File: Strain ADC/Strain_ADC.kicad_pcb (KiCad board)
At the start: 2 copper layers, 40.5 x 23.2 mm, 82 parts, among them J11 Conn_01x05, U1 MCP3421A0T-ECH, U2 MCP3421A0T-ECH, U3 MCP3421A0T-ECH, U4 MCP3421A0T-ECH, U5 MCP3421A0T-ECH, U6 TCA9548APWR, U7 ADC081C021CIMM

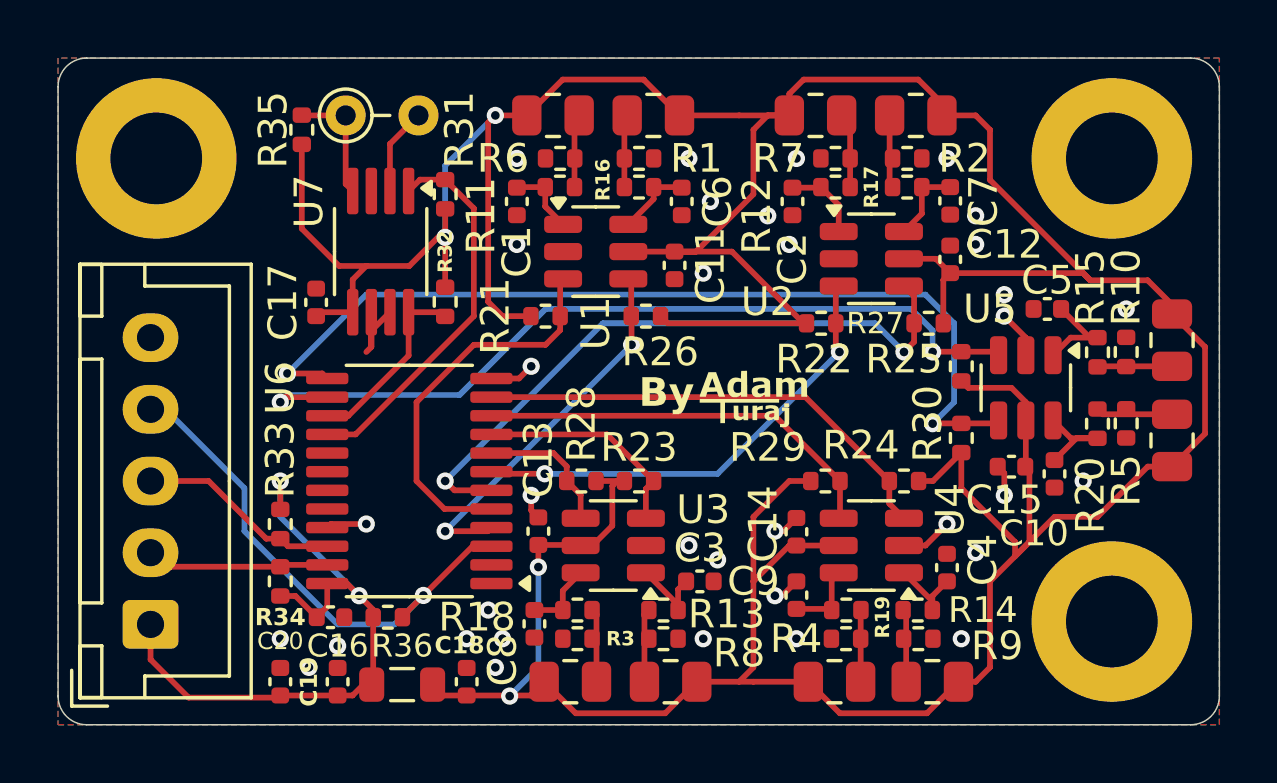
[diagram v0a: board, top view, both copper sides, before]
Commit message: Add part numbers to remaining PCBs, change part numbers on sensor board, redo strain adc layout
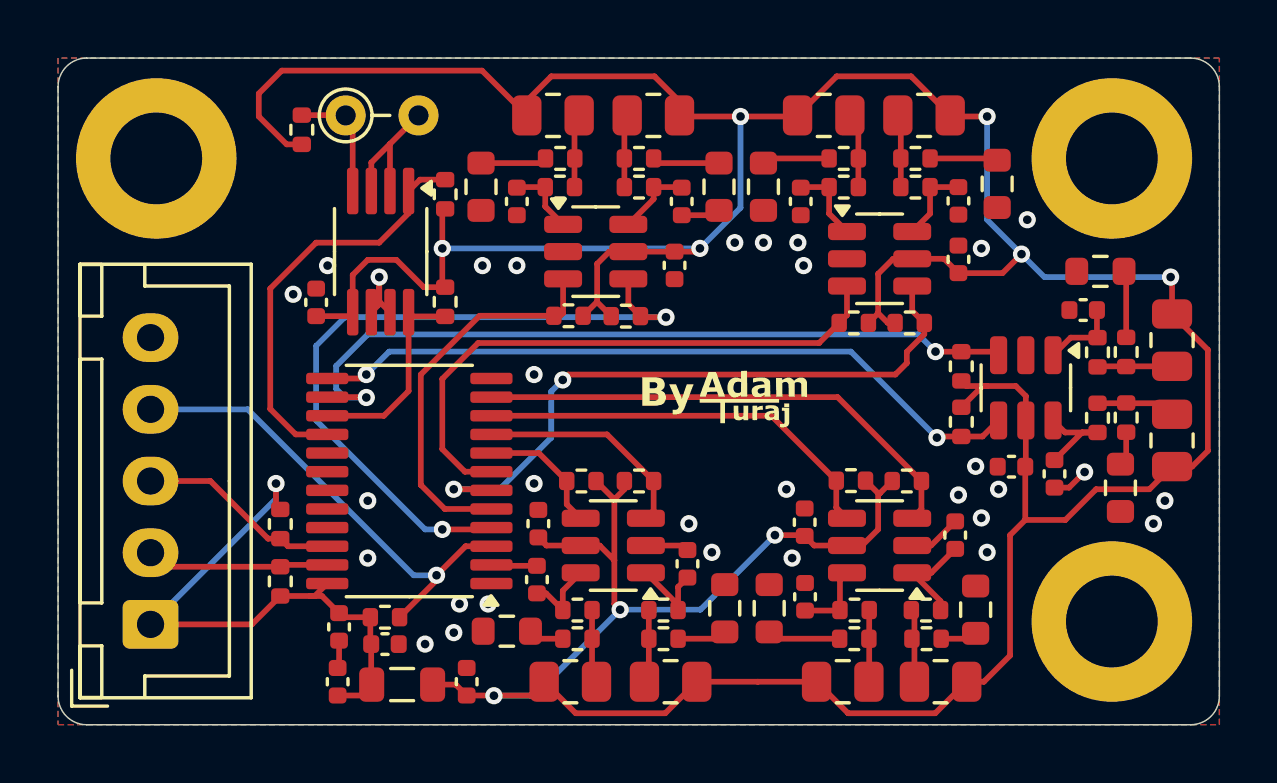
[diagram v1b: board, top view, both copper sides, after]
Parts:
- added R37: 2R, Resistor_SMD:R_0603_1608Metric, F.Cu at (153.4, 111.8)
- added R38: 2R, Resistor_SMD:R_0603_1608Metric, F.Cu at (145.8, 112.5)
- added R39: 2R, Resistor_SMD:R_0603_1608Metric, F.Cu at (167.2, 107.5)
- added R40: 2R, Resistor_SMD:R_0603_1608Metric, F.Cu at (166.6, 100.0)
- added R41: 2R, Resistor_SMD:R_0603_1608Metric, F.Cu at (155.0, 111.8)
- added R42: 2R, Resistor_SMD:R_0603_1608Metric, F.Cu at (162.2, 111.8)
- added R43: 2R, Resistor_SMD:R_0603_1608Metric, F.Cu at (162.9, 97.0)
- added R44: 2R, Resistor_SMD:R_0603_1608Metric, F.Cu at (154.8, 97.0)
- added R45: 2R, Resistor_SMD:R_0603_1608Metric, F.Cu at (153.2, 97.0)
- added R46: 2R, Resistor_SMD:R_0603_1608Metric, F.Cu at (144.9, 97.0)
- R3, R8: value 350R -> 348R
- moved C20 3.88 mm to (141.6, 113.0), turned to 180 degrees
- moved C8 1.54 mm to (146.9, 110.8), turned to 90 degrees
- moved C5 1.25 mm to (165.9, 101.3)
- moved C4 1.17 mm to (161.5, 109.2)
- moved R22 1.14 mm to (157.9, 101.8), turned to 180 degrees
- moved R29 0.89 mm to (157.8, 107.3), turned to 180 degrees
- moved R21 0.80 mm to (148.0, 101.5), turned to 180 degrees
- moved C3 0.75 mm to (152.2, 110.2), turned to 90 degrees
- moved R26 0.70 mm to (150.0, 101.6), turned to 0 degrees
- moved R27 0.66 mm to (159.9, 101.8), turned to 0 degrees
- moved R30 0.56 mm to (161.7, 105.2), turned to -90 degrees
- moved C16 0.45 mm to (140.0, 112.4), turned to -90 degrees
- moved C14 0.44 mm to (156.2, 108.8)
- moved C9 0.31 mm to (156.2, 111.3)
- moved R9 0.29 mm to (160.5, 112.8)
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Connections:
- R1 pad 2: GND -> Net-(R1-Pad2)
- R10 pad 2: GND -> Net-(R10-Pad2)
- R2 pad 2: GND -> Net-(R2-Pad2)
- R3 pad 2: GND -> Net-(R3-Pad2)
- R4 pad 2: GND -> Net-(R4-Pad2)
- R5 pad 2: GND -> Net-(R39-Pad1)
- R6 pad 2: GND -> Net-(R46-Pad1)
- R7 pad 2: GND -> Net-(R44-Pad1)
- R8 pad 2: GND -> Net-(R37-Pad1)
- R9 pad 2: GND -> Net-(R42-Pad1)
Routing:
- net Net-(U1-SDA): track 13.2 -> 25.3 mm
- net Net-(U5-SDA): track 32.4 -> 25.3 mm
- net +3.3VA: track 163.6 -> 158.1 mm, vias 4 -> 9
- net Net-(U2-SCL): track 16.3 -> 20.5 mm, vias 2 -> 0
- net Net-(J11-Pin_1): track 23.3 -> 20.7 mm, vias 2 -> 1
- net Net-(R4-Pad2): track 0.00 -> 2.56 mm
- net Net-(R2-Pad2): track 0.00 -> 2.37 mm
- net Net-(R44-Pad1): track 0.00 -> 2.36 mm
- net Net-(R1-Pad2): track 0.00 -> 2.35 mm
- net Net-(R10-Pad2): track 0.00 -> 2.33 mm
- net Net-(R46-Pad1): track 0.00 -> 2.32 mm
- net Net-(U5-SCL): track 29.2 -> 27.2 mm
- net Net-(R37-Pad1): track 0.00 -> 1.73 mm
- net Net-(J11-Pin_4): track 18.1 -> 16.7 mm
- net Net-(R42-Pad1): track 0.00 -> 1.28 mm
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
